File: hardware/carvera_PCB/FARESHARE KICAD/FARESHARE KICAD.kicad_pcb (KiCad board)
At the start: 2 copper layers, 70 x 54 mm, 14 parts, among them J1 0022232041, J2 0022232041, J3 0022232041, J4 22-23-2021, J5 PJ-102A

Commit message: added silk screen
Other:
- board text added: "FARESHARE v2.0"
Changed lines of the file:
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@@
 		(descr "http://www.molex.com/pdm_docs/sd/022232031_sd.pdf")
 		(property "Reference" "J3"
-			(at 4.33 -4.56 360)
+			(at 4.33 -4.56 0)
 			(layer "F.SilkS")
 			(effects
@@
 		)
 		(property "Value" "0022232041"
-			(at 4.08 4.52 360)
+			(at 4.08 4.52 0)
 			(layer "F.Fab")
 			(effects
@@
 		)
 		(fp_text user "${REFERENCE}"
-			(at 4.17 0 360)
+			(at 4.17 0 0)
 			(layer "F.Fab")
 			(effects
@@
 		(descr "http://www.te.com/commerce/DocumentDelivery/DDEController?Action=srchrtrv&DocNm=1825910&DocType=Customer+Drawing&DocLang=English")
 		(property "Reference" "S1"
-			(at 3.81 -2.3368 270)
+			(at 3.81 -2.3368 -90)
 			(layer "F.SilkS")
 			(effects
@@
 		)
 		(property "Value" "1825910-6"
-			(at 3.6322 7.0866 270)
+			(at 3.6322 7.0866 -90)
 			(layer "F.Fab")
 			(effects
@@
 		)
 		(fp_text user "${REFERENCE}"
-			(at 3.3782 2.286 270)
+			(at 3.3782 2.286 -90)
 			(layer "F.Fab")
 			(effects
@@
 		(descr "http://www.molex.com/pdm_docs/sd/022232031_sd.pdf")
 		(property "Reference" "J4"
-			(at 1.45 -4.48 360)
+			(at 1.45 -4.48 0)
 			(layer "F.SilkS")
 			(effects
@@
 		)
 		(property "Value" "22-23-2021"
-			(at 1.23 4.72 360)
+			(at 1.23 4.72 0)
 			(layer "F.Fab")
 			(effects
@@
 		)
 		(fp_text user "${REFERENCE}"
-			(at 1.25 0.03 360)
+			(at 1.25 0.03 0)
 			(layer "F.Fab")
 			(effects
@@
 		(at 92.5 56.5 90)
 		(property "Reference" "J5"
-			(at 0 -12.1 270)
+			(at 5 5.5 -90)
 			(layer "F.SilkS")
 			(effects
@@
 		)
 		(property "Value" "PJ-102A"
-			(at 0 5.8 270)
+			(at 0 5.8 -90)
 			(layer "F.Fab")
 			(effects
@@
 		(tags "Arduino UNO R2")
 		(property "Reference" "A3"
-			(at 1.27 -3.81 180)
+			(at -0.28 2.76 180)
 			(layer "F.SilkS")
+			(hide yes)
 			(effects
 				(font
@@
 		(layer "Edge.Cuts")
 	)
+	(gr_text "FARESHARE v2.0"
+		(at 147.5 67.5 90)
+		(layer "F.SilkS")
+		(effects
+			(font
+				(size 1 1)
+				(thickness 0.1)
+			)
+			(justify left bottom)
+		)
+	)
 	(segment

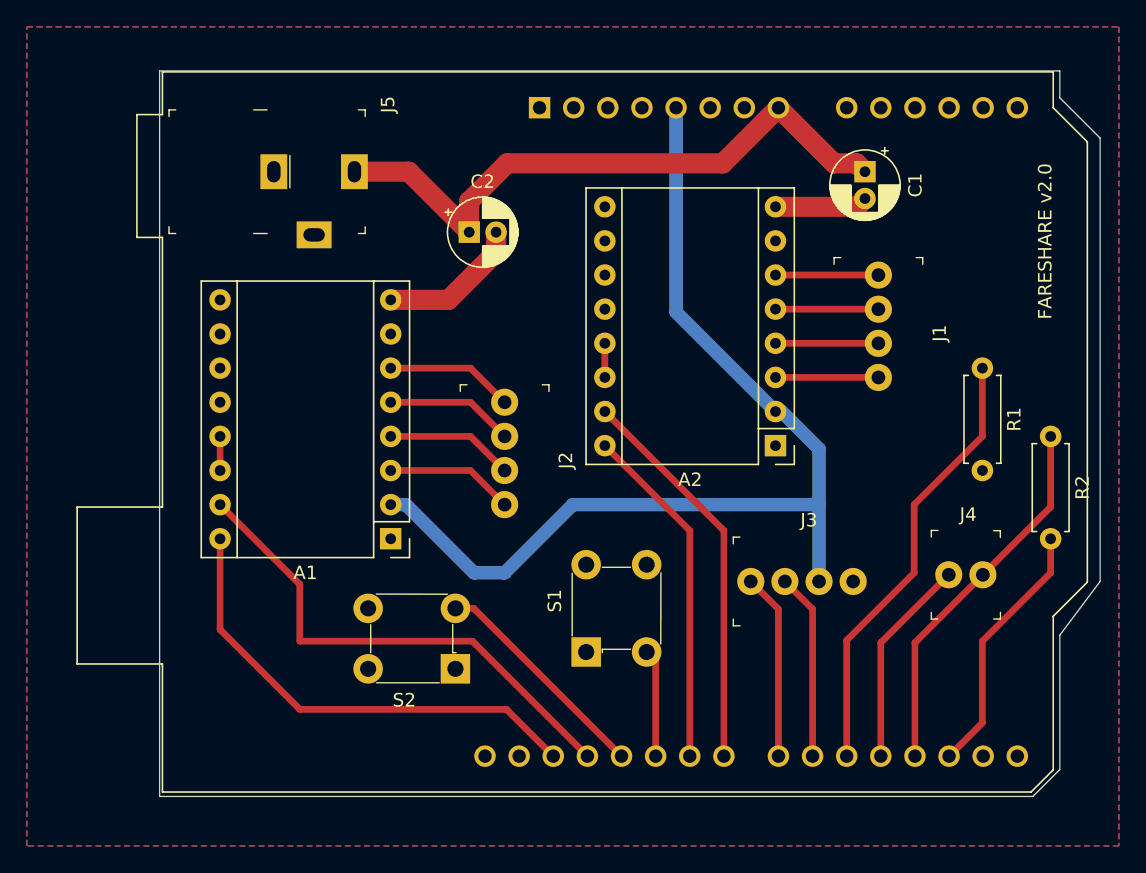
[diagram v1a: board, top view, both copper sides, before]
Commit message: gerbber files updated with a single sided pcb
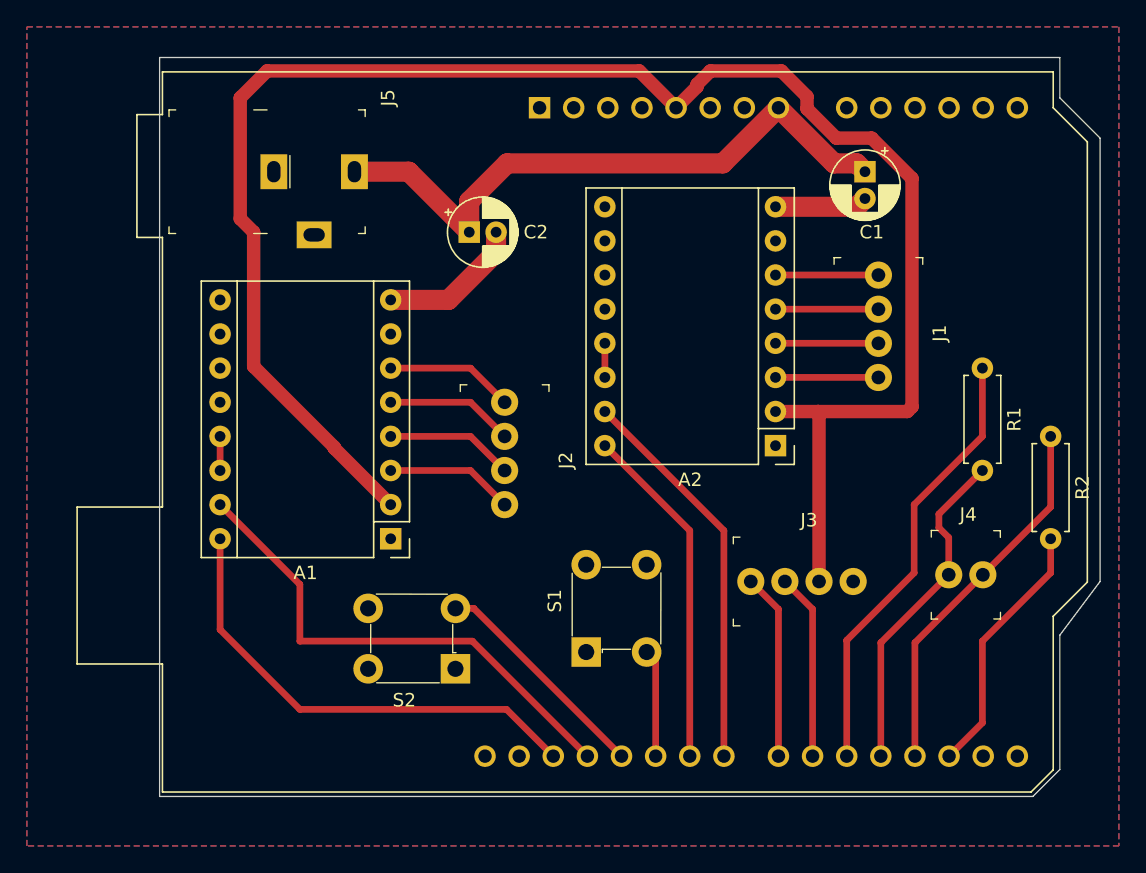
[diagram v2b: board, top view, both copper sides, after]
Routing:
- net +5V: track 76.0 -> 132.4 mm
- net D4: track 15.6 -> 25.0 mm
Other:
- board size 70 x 54 mm -> 70 x 55 mm
- board text removed: "FARESHARE v2.0"
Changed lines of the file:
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@@
 		(descr "http://www.molex.com/pdm_docs/sd/022232031_sd.pdf")
 		(property "Reference" "J3"
-			(at 4.33 -4.56 0)
+			(at 4.33 -4.56 360)
 			(layer "F.SilkS")
 			(effects
@@
 		)
 		(property "Value" "0022232041"
-			(at 4.08 4.52 0)
+			(at 4.08 4.52 360)
 			(layer "F.Fab")
 			(effects
@@
 		)
 		(fp_text user "${REFERENCE}"
-			(at 4.17 0 0)
+			(at 4.17 0 360)
 			(layer "F.Fab")
 			(effects
@@
 		(descr "http://www.te.com/commerce/DocumentDelivery/DDEController?Action=srchrtrv&DocNm=1825910&DocType=Customer+Drawing&DocLang=English")
 		(property "Reference" "S1"
-			(at 3.81 -2.3368 -90)
+			(at 3.81 -2.3368 270)
 			(layer "F.SilkS")
 			(effects
@@
 		)
 		(property "Value" "1825910-6"
-			(at 3.6322 7.0866 -90)
+			(at 3.6322 7.0866 270)
 			(layer "F.Fab")
 			(effects
@@
 		)
 		(fp_text user "${REFERENCE}"
-			(at 3.3782 2.286 -90)
+			(at 3.3782 2.286 270)
 			(layer "F.Fab")
 			(effects
@@
 		(descr "http://www.molex.com/pdm_docs/sd/022232031_sd.pdf")
 		(property "Reference" "J4"
-			(at 1.45 -4.48 0)
+			(at 1.45 -4.48 360)
 			(layer "F.SilkS")
 			(effects
@@
 		)
 		(property "Value" "22-23-2021"
-			(at 1.23 4.72 0)
+			(at 1.23 4.72 360)
 			(layer "F.Fab")
 			(effects
@@
 		)
 		(fp_text user "${REFERENCE}"
-			(at 1.25 0.03 0)
+			(at 1.25 0.03 360)
 			(layer "F.Fab")
 			(effects
@@
 		(at 92.5 56.5 90)
 		(property "Reference" "J5"
-			(at 5 5.5 -90)
+			(at 5.5 5.5 270)
 			(layer "F.SilkS")
 			(effects
@@
 		)
 		(property "Value" "PJ-102A"
-			(at 0 5.8 -90)
+			(at 0 5.8 270)
 			(layer "F.Fab")
 			(effects
@@
 		(tags "CP Radial series Radial pin pitch 2.00mm  diameter 5mm Electrolytic Capacitor")
 		(property "Reference" "C2"
-			(at 1 -3.75 0)
+			(at 4.955112 0 0)
 			(layer "F.SilkS")
 			(effects
@@
 		(tags "Arduino UNO R2")
 		(property "Reference" "A3"
-			(at -0.28 2.76 180)
+			(at 1.27 -3.81 180)
 			(layer "F.SilkS")
 			(hide yes)
@@
 		(tags "CP Radial series Radial pin pitch 2.00mm  diameter 5mm Electrolytic Capacitor")
 		(property "Reference" "C1"
-			(at 1 -3.75 90)
+			(at 4.5 -0.5 180)
 			(layer "F.SilkS")
 			(effects
@@
 	)
 	(gr_line
-		(start 81 103)
-		(end 81 49)
+		(start 81 48)
+		(end 81 103)
 		(stroke
 			(width 0.05)
@@
 	)
 	(gr_line
-		(start 148 91)
-		(end 148 101)
+		(start 148 51)
+		(end 148 48)
 		(stroke
 			(width 0.05)
@@
 	)
 	(gr_line
-		(start 148 49)
-		(end 148 51)
+		(start 148 91)
+		(end 148 101)
 		(stroke
 			(width 0.05)
@@
 	)
 	(gr_line
-		(start 81 49)
-		(end 148 49)
+		(start 148 48)
+		(end 81 48)
 		(stroke
 			(width 0.05)
@@
 		(layer "Edge.Cuts")
 	)
-	(gr_text "FARESHARE v2.0"
-		(at 147.5 67.5 90)
-		(layer "F.SilkS")
-		(effects
-			(font
-				(size 1 1)
-				(thickness 0.1)
-			)
-			(justify left bottom)
-		)
-	)
 	(segment
 		(start 85.5 78.74)
@@
 	)
 	(segment
-		(start 127.3 74.35)
-		(end 126.84 74.35)
+		(start 94 77)
+		(end 88 71)
 		(width 1)
-		(layer "B.Cu")
+		(layer "F.Cu")
 		(net 5)
 	)
 	(segment
-		(start 130.08 81.28)
-		(end 130.08 77.13)
+		(start 126.84 74.35)
+		(end 130 74.35)
 		(width 1)
-		(layer "B.Cu")
+		(layer "F.Cu")
 		(net 5)
 	)
 	(segment
-		(start 130.08 87)
-		(end 130.08 81.28)
+		(start 87 51)
+		(end 89 49)
 		(width 1)
-		(layer "B.Cu")
+		(layer "F.Cu")
 		(net 5)
 	)
 	(segment
-		(start 119.44 51.74)
-		(end 119.44 66.95)
+		(start 137 74)
+		(end 137 57)
 		(width 1)
-		(layer "B.Cu")
+		(layer "F.Cu")
+		(net 5)
+	)
+	(segment
+		(start 129.185305 51.814695)
+		(end 129.185305 50.906626)
+		(width 1)
+		(layer "F.Cu")
+		(net 5)
+	)
+	(segment
+		(start 89 49)
+		(end 116.7 49)
+		(width 1)
+		(layer "F.Cu")
+		(net 5)
+	)
+	(segment
+		(start 94 77.08)
+		(end 94 77)
+		(width 1)
+		(layer "F.Cu")
+		(net 5)
+	)
+	(segment
+		(start 88 71)
+		(end 88 61)
+		(width 1)
+		(layer "F.Cu")
+		(net 5)
+	)
+	(segment
+		(start 137 57)
+		(end 134 54)
+		(width 1)
+		(layer "F.Cu")
+		(net 5)
+	)
+	(segment
+		(start 127.278679 49)
+		(end 122 49)
+		(width 1)
+		(layer "F.Cu")
+		(net 5)
+	)
+	(segment
+		(start 87 60)
+		(end 87 51)
+		(width 1)
+		(layer "F.Cu")
+		(net 5)
+	)
+	(segment
+		(start 121 50.18)
+		(end 119.44 51.74)
+		(width 1)
+		(layer "F.Cu")
+		(net 5)
+	)
+	(segment
+		(start 131.37061 54)
+		(end 129.185305 51.814695)
+		(width 1)
+		(layer "F.Cu")
+		(net 5)
+	)
+	(segment
+		(start 134 54)
+		(end 131.37061 54)
+		(width 1)
+		(layer "F.Cu")
+		(net 5)
+	)
+	(segment
+		(start 88 61)
+		(end 87 60)
+		(width 1)
+		(layer "F.Cu")
+		(net 5)
+	)
+	(segment
+		(start 129.185305 50.906626)
+		(end 127.278679 49)
+		(width 1)
+		(layer "F.Cu")
+		(net 5)
+	)
+	(segment
+		(start 130 74.35)
+		(end 136.65 74.35)
+		(width 1)
+		(layer "F.Cu")
+		(net 5)
+	)
+	(segment
+		(start 122 49)
+		(end 121 50)
+		(width 1)
+		(layer "F.Cu")
 		(net 5)
 	)
 	(segment
 		(start 98.2 81.28)
-		(end 99.33137 81.28)
+		(end 94 77.08)
 		(width 1)
-		(layer "B.Cu")
+		(layer "F.Cu")
 		(net 5)
 	)
 	(segment
-		(start 106.68 86.36)
-		(end 111.76 81.28)
+		(start 130.08 87)
+		(end 130.08 74.43)
 		(width 1)
-		(layer "B.Cu")
+		(layer "F.Cu")
 		(net 5)
 	)
 	(segment
-		(start 119.44 66.95)
-		(end 126.84 74.35)
+		(start 130.08 74.43)
+		(end 130 74.35)
 		(width 1)
-		(layer "B.Cu")
+		(layer "F.Cu")
 		(net 5)
 	)
 	(segment
-		(start 104.41137 86.36)
-		(end 106.68 86.36)
+		(start 116.7 49)
+		(end 119.44 51.74)
 		(width 1)
-		(layer "B.Cu")
+		(layer "F.Cu")
 		(net 5)
 	)
 	(segment
-		(start 111.76 81.28)
-		(end 130.08 81.28)
+		(start 136.65 74.35)
+		(end 137 74)
 		(width 1)
-		(layer "B.Cu")
+		(layer "F.Cu")
 		(net 5)
 	)
 	(segment
-		(start 130.08 77.13)
-		(end 127.3 74.35)
+		(start 121 50)
+		(end 121 50.18)
 		(width 1)
-		(layer "B.Cu")
+		(layer "F.Cu")
 		(net 5)
 	)
 	(segment
-		(start 99.33137 81.28)
-		(end 104.41137 86.36)
+		(start 127.3 74.35)
+		(end 126.84 74.35)
 		(width 1)
 		(layer "B.Cu")
@@
 	)
 	(segment
+		(start 139.735 83.735)
+		(end 139.735 86.5)
+		(width 0.5)
+		(layer "F.Cu")
+		(net 31)
+	)
+	(segment
 		(start 134.68 91.555)
 		(end 134.68 100)
@@
 	)
 	(segment
+		(start 139 81.98)
+		(end 139 83)
+		(width 0.5)
+		(layer "F.Cu")
+		(net 31)
+	)
+	(segment
 		(start 139.735 86.5)
 		(end 134.68 91.555)
 		(width 0.5)
 		(layer "F.Cu")
+		(net 31)
+	)
+	(segment
+		(start 142.24 78.74)
+		(end 139 81.98)
+		(width 0.5)
+		(layer "F.Cu")
+		(net 31)
+	)
+	(segment
+		(start 139 83)
+		(end 139.735 83.735)
+		(width 0.5)
+		(layer "F.Cu")

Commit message: updated pcb+ gerber
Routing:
- net +5V: track 132.4 -> 133.0 mm
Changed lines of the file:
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@@
 		(tags "Pololu Breakout")
 		(property "Reference" "A1"
-			(at 6.35 -2.54 180)
+			(at 5.2 -2.54 180)
 			(layer "F.SilkS")
 			(effects
@@
 		(descr "http://www.molex.com/pdm_docs/sd/022232031_sd.pdf")
 		(property "Reference" "J3"
-			(at 4.33 -4.56 360)
+			(at 2 -4.56 360)
 			(layer "F.SilkS")
 			(effects
@@
 	)
 	(segment
+		(start 119 49)
+		(end 127.278679 49)
+		(width 1)
+		(layer "F.Cu")
+		(net 5)
+	)
+	(segment
 		(start 137 74)
 		(end 137 57)
@@
 	(segment
 		(start 89 49)
-		(end 116.7 49)
+		(end 119 49)
 		(width 1)
 		(layer "F.Cu")
@@
 	)
 	(segment
-		(start 127.278679 49)
-		(end 122 49)
-		(width 1)
-		(layer "F.Cu")
-		(net 5)
-	)
-	(segment
 		(start 87 60)
 		(end 87 51)
@@
 	)
 	(segment
-		(start 121 50.18)
-		(end 119.44 51.74)
+		(start 119.44 51.74)
+		(end 119.44 49.44)
 		(width 1)
 		(layer "F.Cu")
@@
 	)
 	(segment
-		(start 129.185305 50.906626)
-		(end 127.278679 49)
+		(start 119.44 49.44)
+		(end 119 49)
 		(width 1)
 		(layer "F.Cu")
@@
 	)
 	(segment
-		(start 130 74.35)
-		(end 136.65 74.35)
+		(start 129.185305 50.906626)
+		(end 127.278679 49)
 		(width 1)
 		(layer "F.Cu")
@@
 	)
 	(segment
-		(start 122 49)
-		(end 121 50)
+		(start 130 74.35)
+		(end 136.65 74.35)
 		(width 1)
 		(layer "F.Cu")
@@
 	)
 	(segment
-		(start 116.7 49)
-		(end 119.44 51.74)
-		(width 1)
-		(layer "F.Cu")
-		(net 5)
-	)
-	(segment
 		(start 136.65 74.35)
 		(end 137 74)
@@
 	)
 	(segment
-		(start 121 50)
-		(end 121 50.18)
-		(width 1)
-		(layer "F.Cu")
-		(net 5)
-	)
-	(segment
 		(start 127.3 74.35)
 		(end 126.84 74.35)
@@
 	)
 	(segment
-		(start 122.92 55.88)
-		(end 127.06 51.74)
-		(width 1.5)
-		(layer "F.Cu")
-		(net 27)
-	)
-	(segment
-		(start 106.864888 55.88)
-		(end 122.92 55.88)
-		(width 1.5)
-		(layer "F.Cu")
-		(net 27)
-	)
-	(segment
-		(start 104.044888 58.7)
-		(end 106.864888 55.88)
+		(start 127 56.5)
+		(end 133.5 56.5)
 		(width 1.5)
 		(layer "F.Cu")
@@
 	)
 	(segment
-		(start 104.044888 61)
-		(end 104.044888 58.7)
+		(start 127.06 56.44)
+		(end 127 56.5)
 		(width 1.5)
 		(layer "F.Cu")
@@
 	)
 	(segment
-		(start 95.5 56.5)
-		(end 99.544888 56.5)
+		(start 127.06 51.74)
+		(end 127.06 56.44)
 		(width 1.5)
 		(layer "F.Cu")
@@
 	)
 	(segment
-		(start 131.2 55.88)
-		(end 132.88 55.88)
+		(start 104.044888 56.544888)
+		(end 104 56.5)
 		(width 1.5)
 		(layer "F.Cu")
@@
 	)
 	(segment
-		(start 99.544888 56.5)
-		(end 104.044888 61)
+		(start 104 56.5)
+		(end 127 56.5)
 		(width 1.5)
 		(layer "F.Cu")
@@
 	)
 	(segment
-		(start 132.88 55.88)
-		(end 133.5 56.5)
+		(start 104.044888 61)
+		(end 104.044888 56.544888)
 		(width 1.5)
 		(layer "F.Cu")
@@
 	)
 	(segment
-		(start 127.06 51.74)
-		(end 131.2 55.88)
+		(start 95.5 56.5)
+		(end 104 56.5)
 		(width 1.5)
 		(layer "F.Cu")

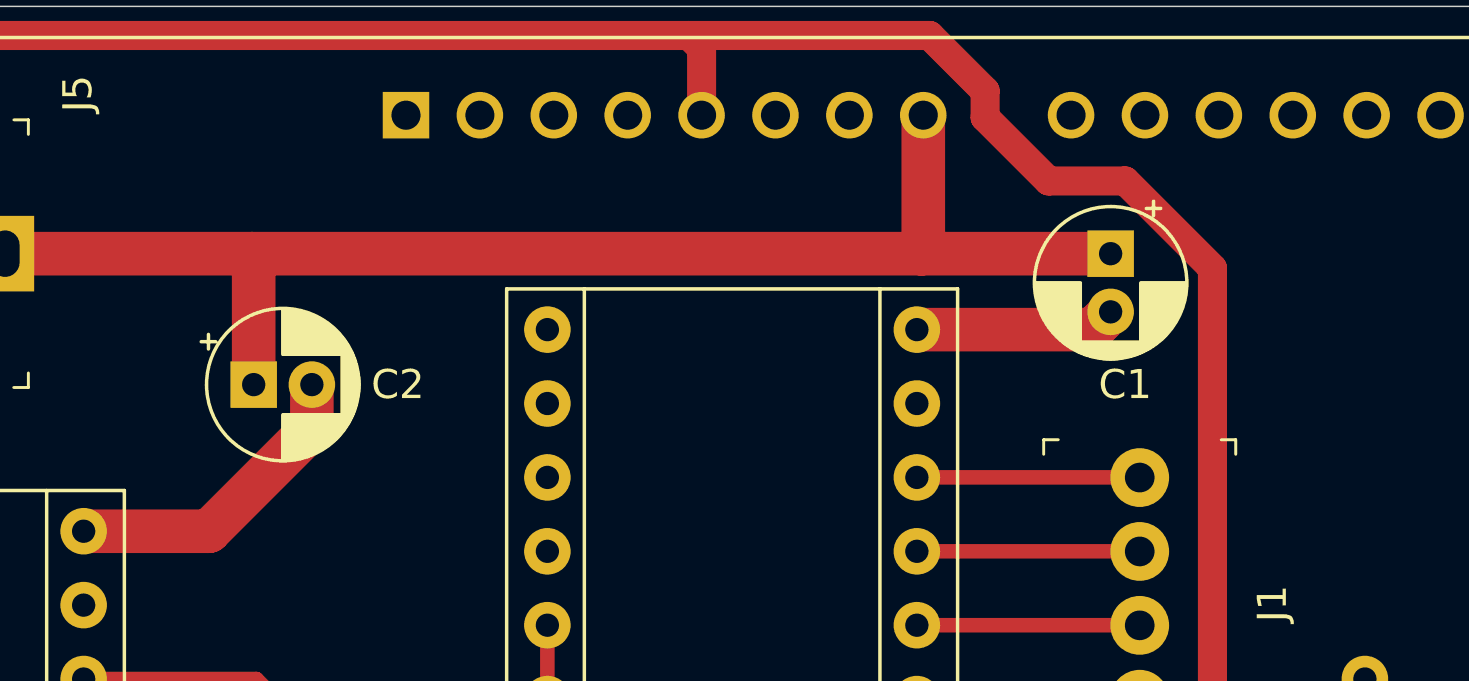
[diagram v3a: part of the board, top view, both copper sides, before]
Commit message: Cap size update
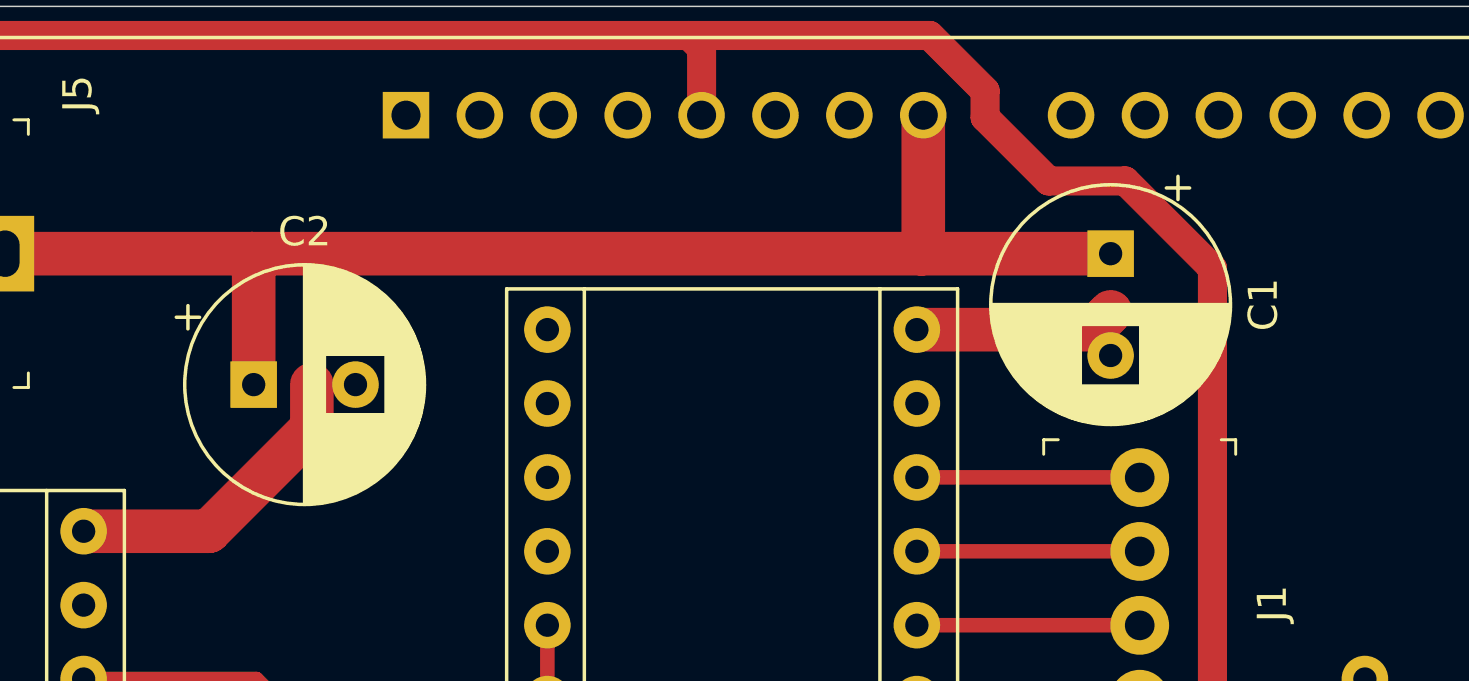
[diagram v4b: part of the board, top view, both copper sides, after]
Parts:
- C1, C2: footprint Capacitor_THT:CP_Radial_D5.0mm_P2.00mm -> Capacitor_THT:CP_Radial_D8.0mm_P3.50mm
